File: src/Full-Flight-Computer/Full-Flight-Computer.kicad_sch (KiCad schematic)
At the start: 36 parts, among them J1 Jumper_NO, P1 1984659, P3 0530470610, P5 B2B-PH-K-SLFSN_JST, U2 STM32H750VBTx, U3 LMS8117AMP-3.3_NOPB, Y1 ECS-240-18-33-JGN-TR

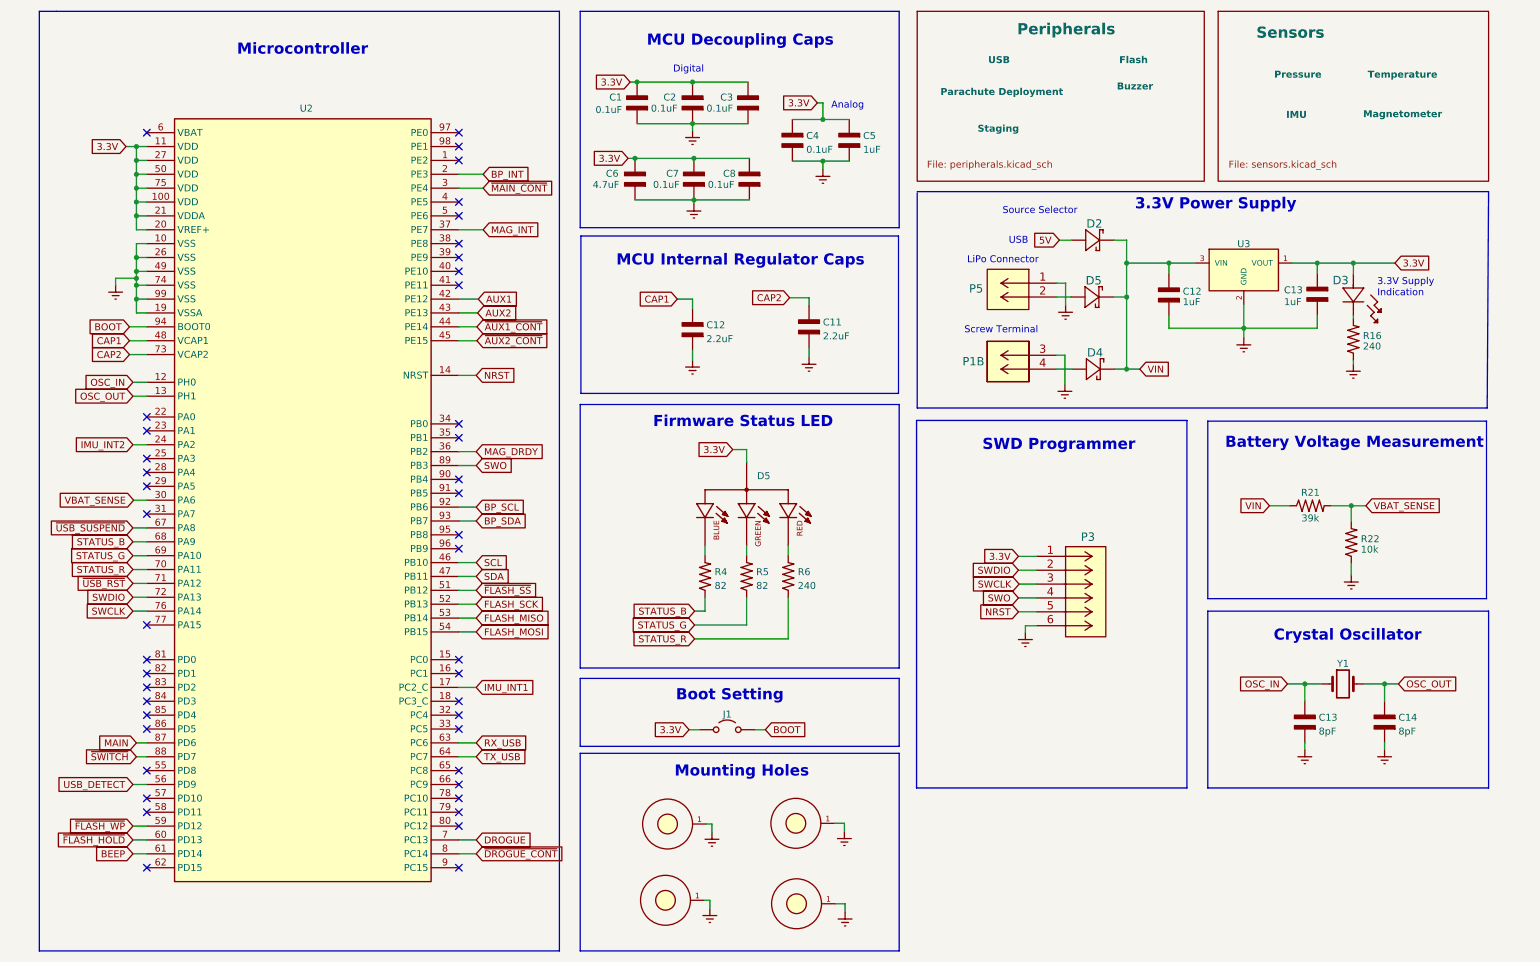
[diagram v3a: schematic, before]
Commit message: implemented high G accelerometer schematic
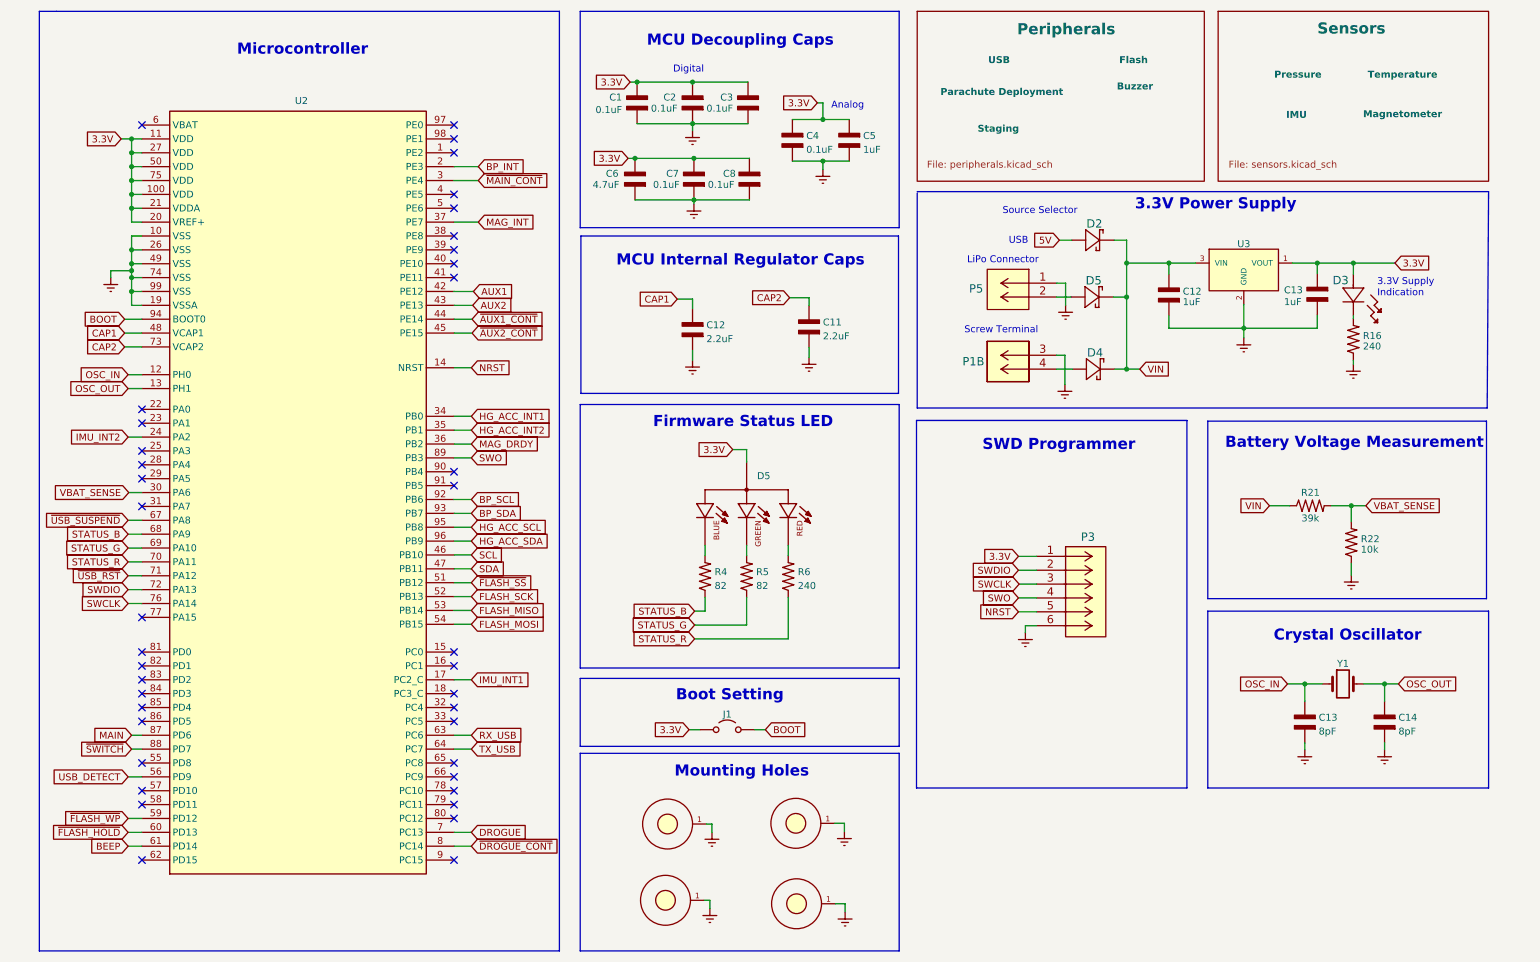
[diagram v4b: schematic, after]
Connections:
- net HG_ACC_INT1: now reaches U2.34 (PB0)
- net HG_ACC_INT2: now reaches U2.35 (PB1)
- net HG_ACC_SCL: now reaches U2.95 (PB8)
- net HG_ACC_SDA: now reaches U2.96 (PB9)
- no-connect marks 44 -> 40
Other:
- moved on the sheet: U2

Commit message: redid component designators and updated BOM
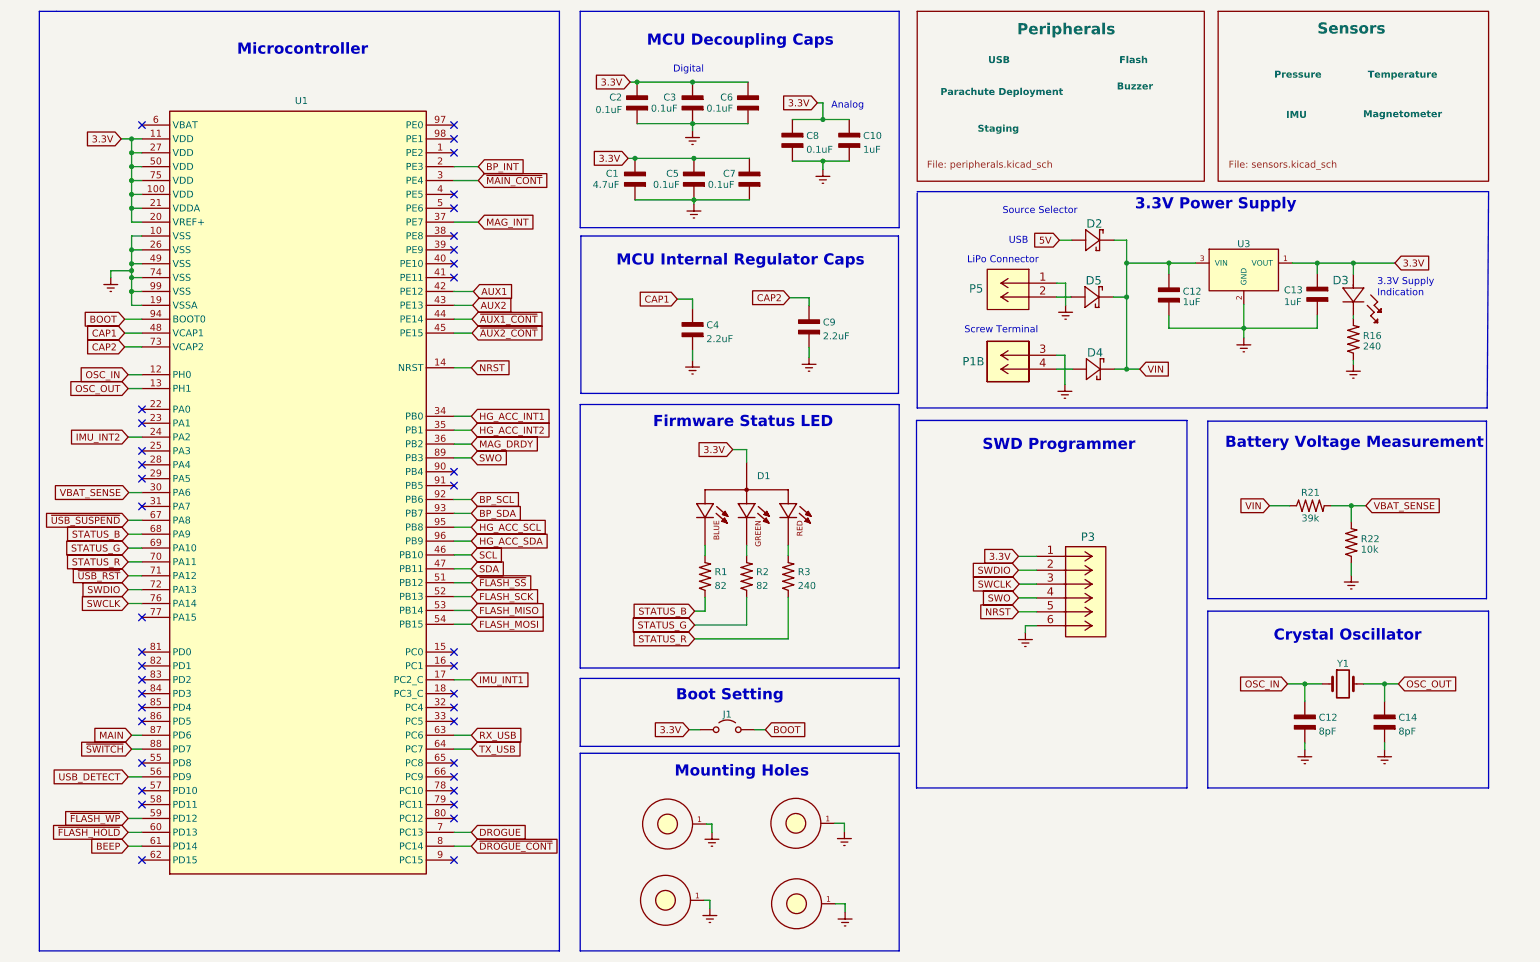
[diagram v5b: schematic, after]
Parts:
- J1: footprint Base-Flight-Computer:Jumper-NO -> Full-Flight-Computer:Jumper-NO
- R2: renamed from R5; footprint Flight-Computer:RES_0603 -> Full-Flight-Computer:RES_0402; symbol Flight-Computer:RES_0603 -> Full-Flight-Computer:RES_0402
- U3: value LMS8117AMP-3.3_NOPB -> AP7370-33Y-13
- renumbered C6 to C1, C5 to C10, C13 to C12, C1 to C2, C2 to C3, C12 to C4, C7 to C5, C3 to C6, C8 to C7, C4 to C8, C11 to C9, D5 to D1, H3 to H1, H1 to H3, R4 to R1, R6 to R3, U2 to U1

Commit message: placed all components on test board
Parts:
- C7: footprint Full-Flight-Computer:CAP_0603 -> Full-Flight-Computer:CAP_0402; symbol Full-Flight-Computer:CAP_0603 -> Full-Flight-Computer:CAP_0402
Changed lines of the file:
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@@
     )
   )
-  (symbol (lib_id "Full-Flight-Computer:CAP_0603") (at 146.558 49.784 90) (unit 1)
+  (symbol (lib_id "Full-Flight-Computer:CAP_0402") (at 146.558 49.784 90) (unit 1)
     (in_bom yes) (on_board yes) (dnp no)
     (property "Reference" "C7" (at 141.732 48.768 90)
@@
       (effects (font (size 1.27 1.27)) (justify right))
     )
-    (property "Footprint" "Full-Flight-Computer:CAP_0603" (at 156.718 52.324 0)
+    (property "Footprint" "Full-Flight-Computer:CAP_0402" (at 156.718 52.324 0)
       (effects (font (size 1.27 1.27)) (justify left bottom) hide)
     )

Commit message: completed initial layout
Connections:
- net AUX1: now also U1.8 (PC14); no longer U1.42 (PE12)
- net AUX2: now also U1.7 (PC13); no longer U1.43 (PE13)
- net DROGUE: now also U1.17 (PC2_C); no longer U1.7 (PC13)
- net HG_ACC_INT1: now also U1.55 (PD8); no longer U1.34 (PB0)
- net HG_ACC_INT2: now also U1.56 (PD9); no longer U1.35 (PB1)
- net IMU_INT1: now also U1.24 (PA2); no longer U1.17 (PC2_C)
- net IMU_INT2: now also U1.25 (PA3); no longer U1.24 (PA2)
- net MAG_DRDY: now also U1.31 (PA7); no longer U1.36 (PB2)
- net MAG_INT: now also U1.32 (PC4); no longer U1.37 (PE7)
- net MAIN: now also U1.16 (PC1); no longer U1.87 (PD6)
- net STATUS_B: now also U1.41 (PE11); no longer U1.68 (PA9)
- net STATUS_G: now also U1.43 (PE13); no longer U1.69 (PA10)
- net STATUS_R: now also U1.39 (PE9); no longer U1.70 (PA11)
- net USB_DETECT: now also U1.57 (PD10); no longer U1.56 (PD9)
- net ~{AUX1_CONT}: now also U1.15 (PC0); no longer U1.44 (PE14)
- net ~{AUX2_CONT}: now also U1.5 (PE6); no longer U1.45 (PE15)
- net ~{DROGUE_CONT}: now also U1.18 (PC3_C); no longer U1.8 (PC14)
- net ~{MAIN_CONT}: now also U1.22 (PA0); no longer U1.3 (PE4)
- net ~{SWITCH}: now also U1.9 (PC15); no longer U1.88 (PD7)

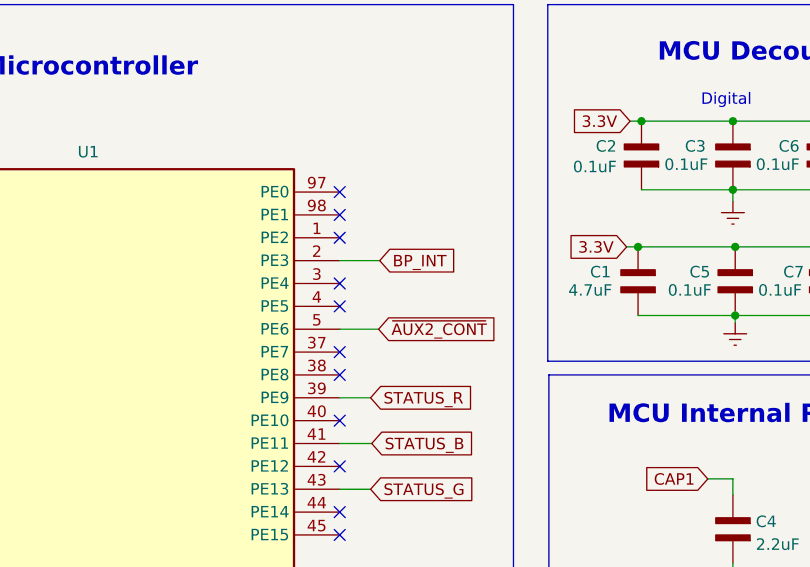
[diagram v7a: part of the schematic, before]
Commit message: moved BP_INT signal to new MCU pin to avoid EXTI collision with IMU interrupt signal
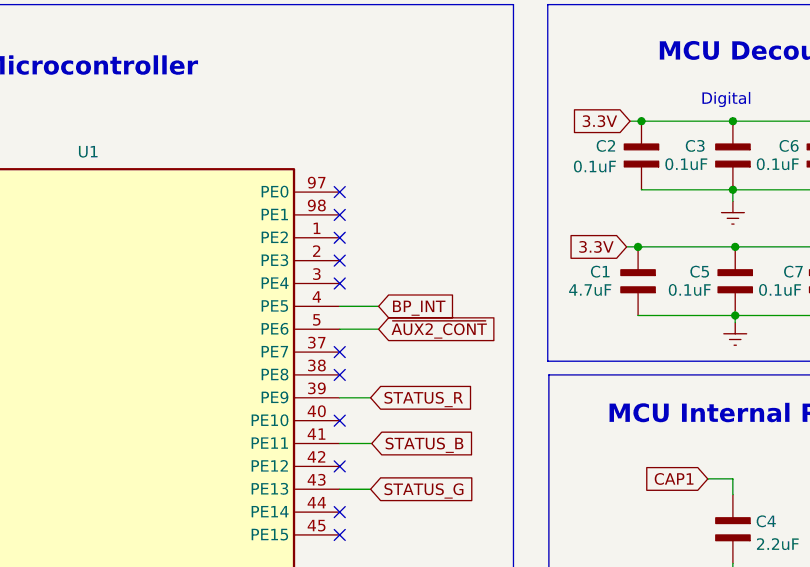
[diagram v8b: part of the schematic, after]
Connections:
- net BP_INT: now also U1.4 (PE5); no longer U1.2 (PE3)
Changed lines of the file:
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@@
   (no_connect (at 35.306 117.348))
   (no_connect (at 92.456 103.378))
-  (no_connect (at 92.456 52.578))
   (no_connect (at 35.306 141.478))
   (no_connect (at 35.306 114.808))
@@
   (no_connect (at 92.456 70.358))
   (no_connect (at 35.306 119.888))
+  (no_connect (at 92.456 47.498))
   (no_connect (at 35.306 174.498))
   (polyline (pts (xy 173.99 91.059) (xy 173.99 139.319))
@@
     (stroke (width 0) (type default))
   )
+  (wire (pts (xy 92.456 52.578) (xy 96.774 52.578))
+    (stroke (width 0) (type default))
+  )
   (wire (pts (xy 35.306 72.898) (xy 33.401 72.898))
     (stroke (width 0) (type default))
@@
   )
   (wire (pts (xy 33.401 55.118) (xy 35.306 55.118))
-    (stroke (width 0) (type default))
-  )
-  (wire (pts (xy 92.456 47.498) (xy 96.901 47.498))
     (stroke (width 0) (type default))
   )
@@
     )
   )
-  (global_label "BP_INT" (shape input) (at 96.901 47.498 0) (fields_autoplaced)
-    (effects (font (size 1.27 1.27)) (justify left))
-    (property "Intersheetrefs" "${INTERSHEET_REFS}" (at 105.6357 47.4186 0)
-      (effects (font (size 1.27 1.27)) (justify left) hide)
-    )
+  (global_label "BP_INT" (shape input) (at 96.774 52.578 0) (fields_autoplaced)
+    (effects (font (size 1.27 1.27)) (justify left))
+    (property "Intersheetrefs" "${INTERSHEET_REFS}" (at 105.5087 52.4986 0)
+      (effects (font (size 1.27 1.27)) (justify left) hide)
+    )
